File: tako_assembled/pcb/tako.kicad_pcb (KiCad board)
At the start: 4 copper layers, 230.7 x 97.8 mm, 146 parts, among them J1 MJ-4PP-9, J101 MJ-4PP-9, J102 OLED, J2 OLED, SW1 EC_SW, SW10 EC_SW, SW101 EC_SW, SW102 EC_SW, SW103 EC_SW, SW104 EC_SW, SW105 EC_SW, SW106 EC_SW, SW107 EC_SW, SW108 EC_SW, SW109 EC_SW, SW11 EC_SW, SW110 EC_SW, SW111 EC_SW, SW112 EC_SW, SW113 EC_SW, SW114 EC_SW, SW115 EC_SW, SW116 EC_SW, SW117 EC_SW, SW12 EC_SW, SW13 EC_SW, SW14 EC_SW, SW15 EC_SW, SW16 EC_SW, SW17 EC_SW, SW2 EC_SW, SW3 EC_SW, SW4 EC_SW, SW5 EC_SW, SW6 EC_SW, SW7 EC_SW, SW8 EC_SW, SW9 EC_SW, U1 STM32F401CBUx, U101 STM32F401CBUx, U102 XC6206PxxxMR, U103 OPA350, U104 74HC4051, U2 XC6206PxxxMR, U3 OPA350, U4 74HC4051, Y1 8 MHz, Y101 8 MHz

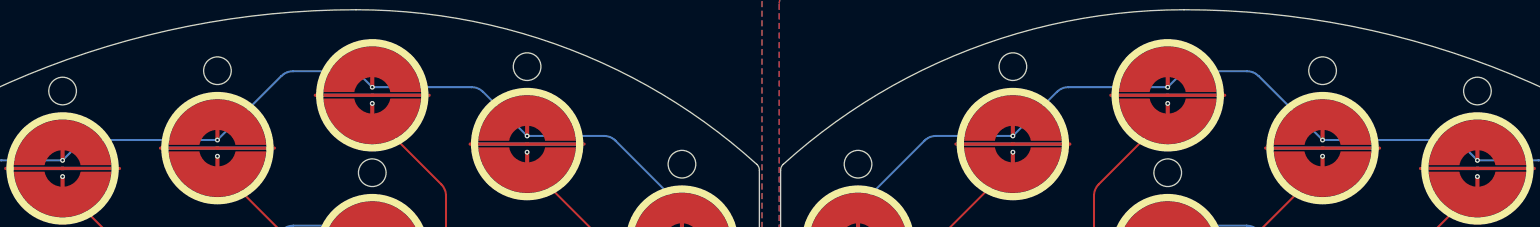
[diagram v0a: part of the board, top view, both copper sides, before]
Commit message: Fix mounting holes and add bottom plate cutouts
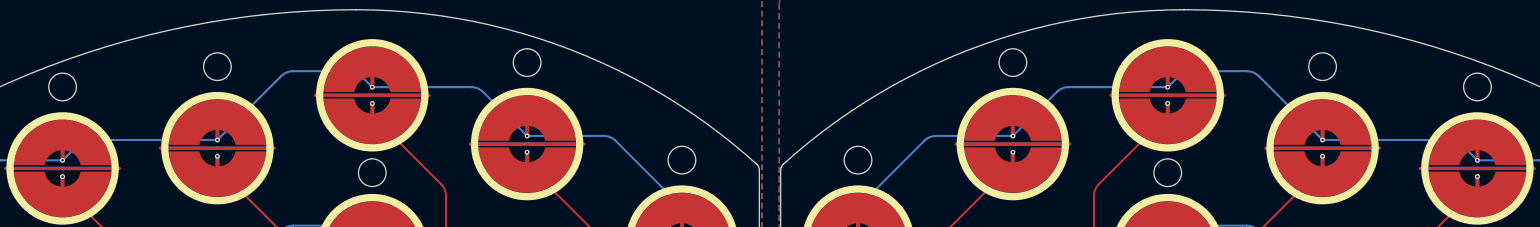
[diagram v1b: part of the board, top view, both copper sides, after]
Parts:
- moved H1 0.50 mm to (158.9, 68.7)
- moved H10 0.50 mm to (235.1, 59.7)
- moved H101 0.50 mm to (137.2, 68.7)
- moved H104 0.50 mm to (118.2, 56.7)
- moved H109 0.50 mm to (80.1, 57.2)
- moved H110 0.50 mm to (61.0, 59.7)
- moved H4 0.50 mm to (178.0, 56.7)
- moved H9 0.50 mm to (216.1, 57.2)
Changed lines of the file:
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@@
     )
     (pad_to_mask_clearance 0)
-    (grid_origin 146.768127 84.211)
+    (grid_origin 235.105483 60.237639)
     (pcbplotparams
       (layerselection 0x00010fc_ffffffff)
@@
   )
   (footprint "local:MountingHole_3.4mm" (layer "F.Cu")
-    (at 216.055485 57.737644)
+    (at 216.055485 57.237644)
     (descr "Mounting Hole 2.2mm, no annular, M2")
     (tags "mounting hole 2.2mm no annular m2")
@@
   )
   (footprint "local:MountingHole_3.4mm" (layer "F.Cu")
-    (at 235.105483 60.237639)
+    (at 235.105483 59.737639)
     (descr "Mounting Hole 2.2mm, no annular, M2")
     (tags "mounting hole 2.2mm no annular m2")
@@
   )
   (footprint "local:MountingHole_3.4mm" (layer "F.Cu")
-    (at 177.95548 57.238145)
+    (at 177.95548 56.738145)
     (descr "Mounting Hole 2.2mm, no annular, M2")
     (tags "mounting hole 2.2mm no annular m2")
@@
   )
   (footprint "local:MountingHole_3.4mm" (layer "F.Cu")
-    (at 158.905476 69.238141)
+    (at 158.905476 68.738141)
     (descr "Mounting Hole 2.2mm, no annular, M2")
     (tags "mounting hole 2.2mm no annular m2")
@@
   )
   (footprint "local:MountingHole_3.4mm" (layer "B.Cu")
-    (at 61.04288 60.237639 180)
+    (at 61.04288 59.737639 180)
     (descr "Mounting Hole 2.2mm, no annular, M2")
     (tags "mounting hole 2.2mm no annular m2")
@@
   )
   (footprint "local:MountingHole_3.4mm" (layer "B.Cu")
-    (at 118.192883 57.238145 180)
+    (at 118.192883 56.738145 180)
     (descr "Mounting Hole 2.2mm, no annular, M2")
     (tags "mounting hole 2.2mm no annular m2")
@@
   )
   (footprint "local:MountingHole_3.4mm" (layer "B.Cu")
-    (at 80.092878 57.737644 180)
+    (at 80.092878 57.237644 180)
     (descr "Mounting Hole 2.2mm, no annular, M2")
     (tags "mounting hole 2.2mm no annular m2")
@@
   )
   (footprint "local:MountingHole_3.4mm" (layer "B.Cu")
-    (at 137.242887 69.238141 180)
+    (at 137.242887 68.738141 180)
     (descr "Mounting Hole 2.2mm, no annular, M2")
     (tags "mounting hole 2.2mm no annular m2")
